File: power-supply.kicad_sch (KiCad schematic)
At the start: 107 parts, among them J10 Molex_Pico-Lock_1x2_504050-02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, J5 Molex_Pico-Lock_1x2_504050-02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, Q1 BSS138PW, Q2 BSS138PW, Q3 BSS138PW, Q4 BSS138PW, Q5 BSS138PW, Q6 BSS138PW, U10 TPS62823DLCT, U11 TPS62823DLCT, U12 TPS62823DLCT, U13 TPS62823DLCT, U16 TPS62823DLCT, U25 TPS54561QDPRRQ1, U9 LM3881

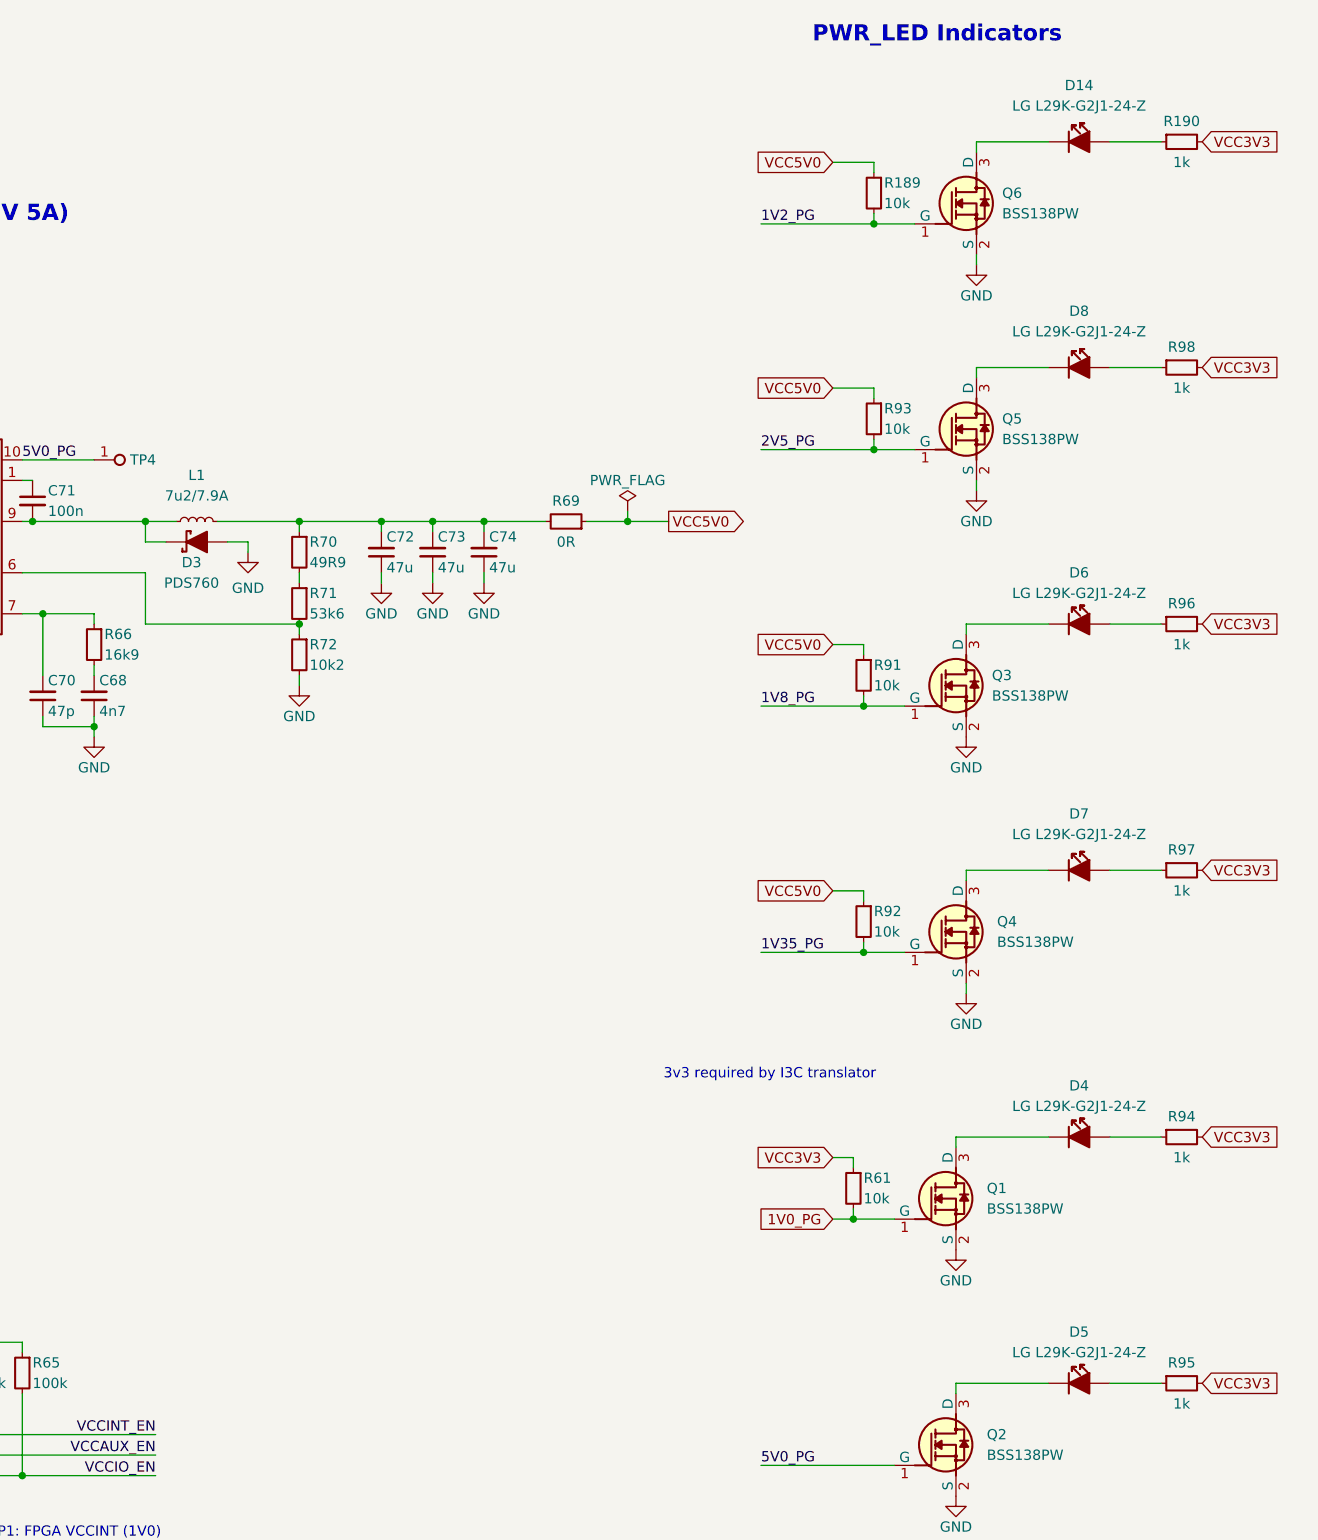
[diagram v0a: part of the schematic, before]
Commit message: [#68236] Update symbols and footprints, clean ERC and DRC
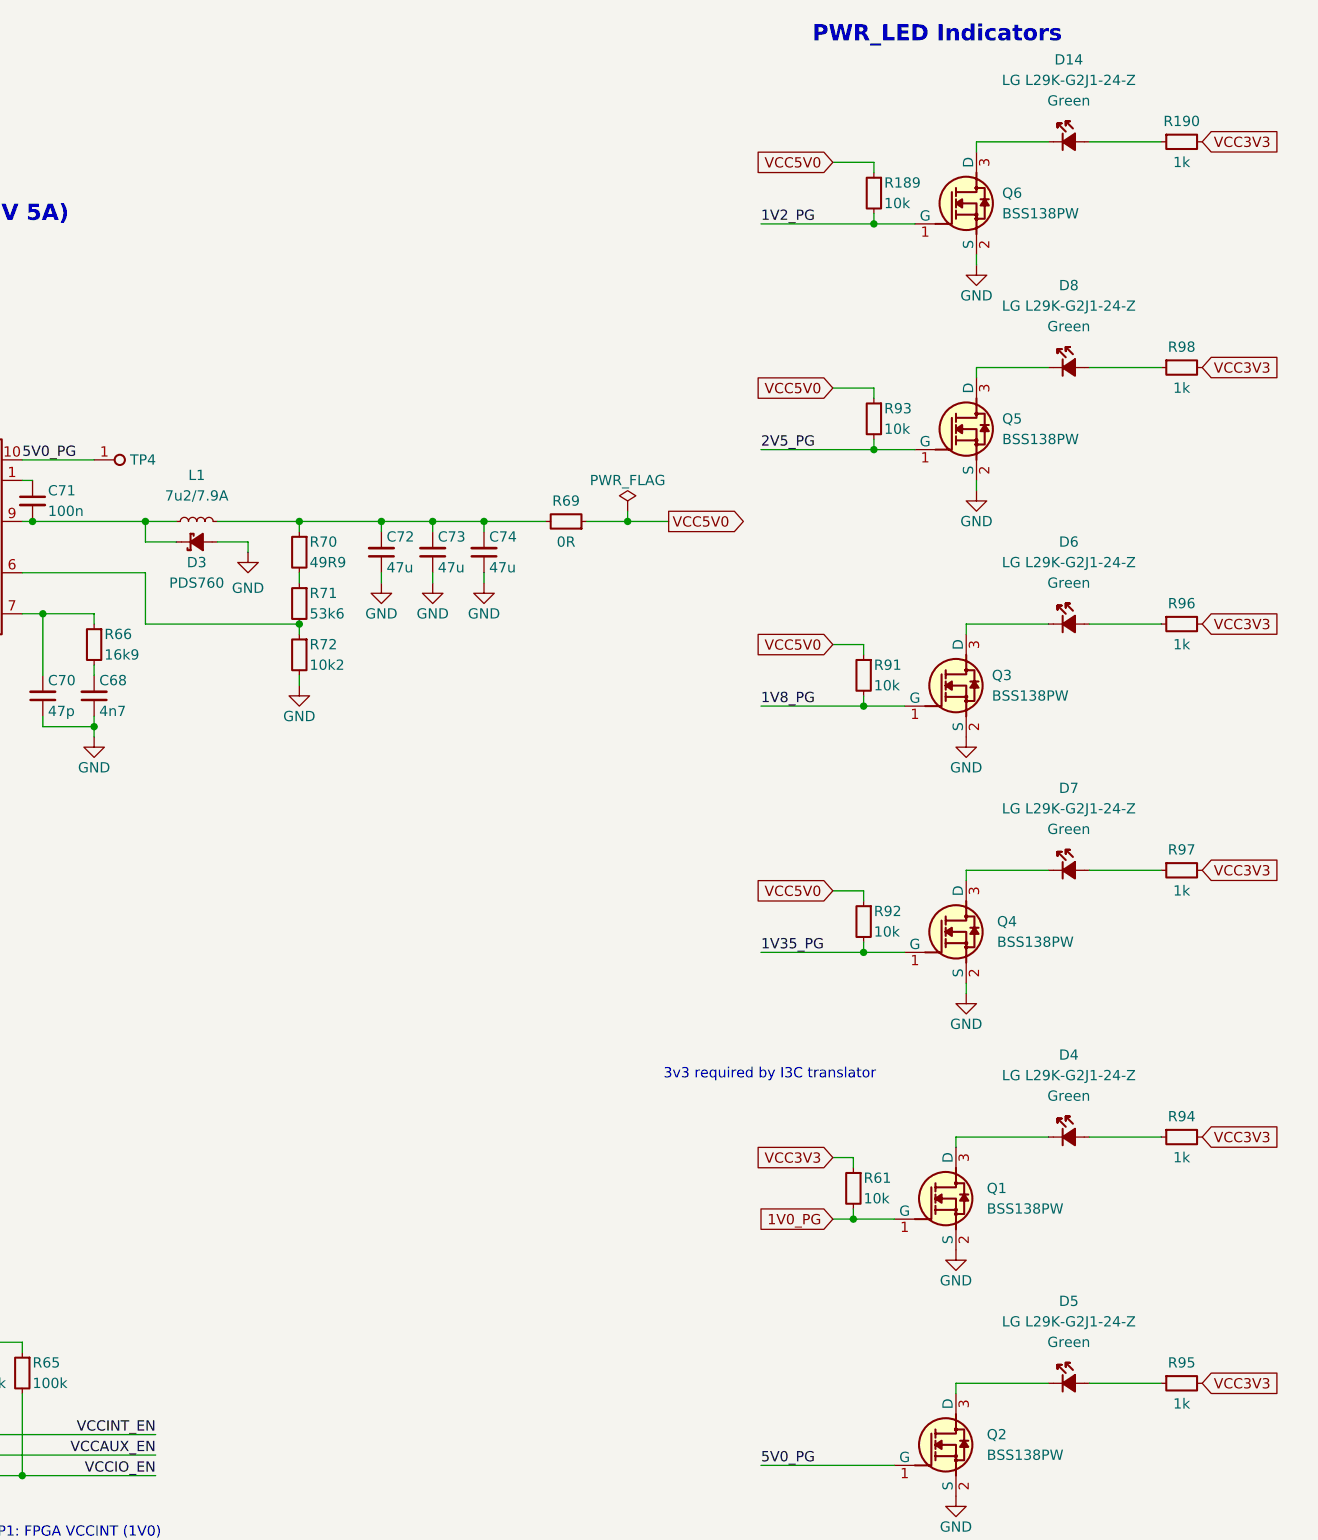
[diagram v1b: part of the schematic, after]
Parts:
- C2, C75, C76, C77, C78: Dielectric (none) -> template_dielectric
- C3, C79, C80, C81, C82: Dielectric (none) -> C0G; Voltage (none) -> 100V
- C65, C66, C67, C71: Public (none) -> False
- D14, D4, D5, D6, D7, D8: Color (none) -> Green
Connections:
- net GND: now also D3.2 (A); no longer D3.A
- net at R190.1: now also D14.2 (A); no longer D14.1
- net at Q6.3 (D): now also D14.1 (C); no longer D14.2
- net at Q3.3 (D): now also D6.1 (C); no longer D6.2
- net at Q4.3 (D): now also D7.1 (C); no longer D7.2
- net at Q1.3 (D): now also D4.1 (C); no longer D4.2
- net at Q2.3 (D): now also D5.1 (C); no longer D5.2
- net at Q5.3 (D): now also D8.1 (C); no longer D8.2
- net at C71.2, L1.1, U25.9 (SW): now also D3.1 (C); no longer D3.C
- net at R98.1: now also D8.2 (A); no longer D8.1
- net at R96.1: now also D6.2 (A); no longer D6.1
- net at R97.1: now also D7.2 (A); no longer D7.1
- net at R94.1: now also D4.2 (A); no longer D4.1
- net at R95.1: now also D5.2 (A); no longer D5.1

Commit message: [#82378] Project refresh 81589
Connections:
- net GND: now also J10.MP1 (MP), J10.MP2, J5.MP1 (MP), J5.MP2; no longer J10.SH, J5.SH
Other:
- moved on the sheet: C14, C15, C16, C65, C66, C67, R187, R190, R72, R74, R76, R78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

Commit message: a lot of routing and almost all caps of the fpga are placed down
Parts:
- C101, C103, C250, C3, C64, C68, C69, C70, C71, C79, C80, C81, C82, C83, C84, C85, C86, C87, C88, C89, C90: footprint antmicro-footprints:C_0402_1005Metric -> Capacitor_SMD:C_0402_1005Metric
- C14, C15, C16, C2, C65, C66, C67, C72, C73, C74, C75, C76, C77, C78: footprint antmicro-footprints:C_0603_1608Metric -> Capacitor_SMD:C_0603_1608Metric
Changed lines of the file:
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@@
 			)
 		)
-		(property "Footprint" "antmicro-footprints:C_0603_1608Metric"
+		(property "Footprint" "Capacitor_SMD:C_0603_1608Metric"
 			(at 328.93 187.96 0)
 			(hide yes)
@@
 			)
 		)
-		(property "Footprint" "antmicro-footprints:C_0402_1005Metric"
+		(property "Footprint" "Capacitor_SMD:C_0402_1005Metric"
 			(at 365.76 198.12 0)
 			(hide yes)
@@
 			)
 		)
-		(property "Footprint" "antmicro-footprints:C_0402_1005Metric"
+		(property "Footprint" "Capacitor_SMD:C_0402_1005Metric"
 			(at 382.27 198.12 0)
 			(hide yes)
@@
 			)
 		)
-		(property "Footprint" "antmicro-footprints:C_0402_1005Metric"
+		(property "Footprint" "Capacitor_SMD:C_0402_1005Metric"
 			(at 389.89 198.12 0)
 			(hide yes)
@@
 			)
 		)
-		(property "Footprint" "antmicro-footprints:C_0402_1005Metric"
+		(property "Footprint" "Capacitor_SMD:C_0402_1005Metric"
 			(at 74.93 187.96 0)
 			(hide yes)
@@
 			)
 		)
-		(property "Footprint" "antmicro-footprints:C_0603_1608Metric"
+		(property "Footprint" "Capacitor_SMD:C_0603_1608Metric"
 			(at 87.63 43.18 0)
 			(hide yes)
@@
 			)
 		)
-		(property "Footprint" "antmicro-footprints:C_0603_1608Metric"
+		(property "Footprint" "Capacitor_SMD:C_0603_1608Metric"
 			(at 93.98 43.18 0)
 			(hide yes)
@@
 			)
 		)
-		(property "Footprint" "antmicro-footprints:C_0603_1608Metric"
+		(property "Footprint" "Capacitor_SMD:C_0603_1608Metric"
 			(at 100.33 43.18 0)
 			(hide yes)
@@
 			)
 		)
-		(property "Footprint" "antmicro-footprints:C_0402_1005Metric"
+		(property "Footprint" "Capacitor_SMD:C_0402_1005Metric"
 			(at 101.6 69.85 0)
 			(hide yes)
@@
 			)
 		)
-		(property "Footprint" "antmicro-footprints:C_0402_1005Metric"
+		(property "Footprint" "Capacitor_SMD:C_0402_1005Metric"
 			(at 142.24 85.09 0)
 			(hide yes)
@@
 			)
 		)
-		(property "Footprint" "antmicro-footprints:C_0402_1005Metric"
+		(property "Footprint" "Capacitor_SMD:C_0402_1005Metric"
 			(at 135.89 85.09 0)
 			(hide yes)
@@
 			)
 		)
-		(property "Footprint" "antmicro-footprints:C_0402_1005Metric"
+		(property "Footprint" "Capacitor_SMD:C_0402_1005Metric"
 			(at 109.22 96.52 0)
 			(hide yes)
@@
 			)
 		)
-		(property "Footprint" "antmicro-footprints:C_0603_1608Metric"
+		(property "Footprint" "Capacitor_SMD:C_0603_1608Metric"
 			(at 177.8 67.31 0)
 			(hide yes)
@@
 			)
 		)
-		(property "Footprint" "antmicro-footprints:C_0603_1608Metric"
+		(property "Footprint" "Capacitor_SMD:C_0603_1608Metric"
 			(at 184.15 67.31 0)
 			(hide yes)
@@
 			)
 		)
-		(property "Footprint" "antmicro-footprints:C_0603_1608Metric"
+		(property "Footprint" "Capacitor_SMD:C_0603_1608Metric"
 			(at 190.5 67.31 0)
 			(hide yes)
@@
 			)
 		)
-		(property "Footprint" "antmicro-footprints:C_0603_1608Metric"
+		(property "Footprint" "Capacitor_SMD:C_0603_1608Metric"
 			(at 328.93 10.16 0)
 			(hide yes)
@@
 			)
 		)
-		(property "Footprint" "antmicro-footprints:C_0603_1608Metric"
+		(property "Footprint" "Capacitor_SMD:C_0603_1608Metric"
 			(at 57.15 43.18 0)
 			(hide yes)
@@
 			)
 		)
-		(property "Footprint" "antmicro-footprints:C_0603_1608Metric"
+		(property "Footprint" "Capacitor_SMD:C_0603_1608Metric"
 			(at 67.31 43.18 0)
 			(hide yes)
@@
 			)
 		)
-		(property "Footprint" "antmicro-footprints:C_0603_1608Metric"
+		(property "Footprint" "Capacitor_SMD:C_0603_1608Metric"
 			(at 77.47 43.18 0)
 			(hide yes)
@@
 			)
 		)
-		(property "Footprint" "antmicro-footprints:C_0402_1005Metric"
+		(property "Footprint" "Capacitor_SMD:C_0402_1005Metric"
 			(at 365.76 20.32 0)
 			(hide yes)
@@
 			)
 		)
-		(property "Footprint" "antmicro-footprints:C_0402_1005Metric"
+		(property "Footprint" "Capacitor_SMD:C_0402_1005Metric"
 			(at 85.09 187.96 0)
 			(hide yes)
@@
 			)
 		)
-		(property "Footprint" "antmicro-footprints:C_0402_1005Metric"
+		(property "Footprint" "Capacitor_SMD:C_0402_1005Metric"
 			(at 382.27 20.32 0)
 			(hide yes)
@@
 			)
 		)
-		(property "Footprint" "antmicro-footprints:C_0402_1005Metric"
+		(property "Footprint" "Capacitor_SMD:C_0402_1005Metric"
 			(at 389.89 20.32 0)
 			(hide yes)
@@
 			)
 		)
-		(property "Footprint" "antmicro-footprints:C_0603_1608Metric"
+		(property "Footprint" "Capacitor_SMD:C_0603_1608Metric"
 			(at 328.93 54.61 0)
 			(hide yes)
@@
 			)
 		)
-		(property "Footprint" "antmicro-footprints:C_0402_1005Metric"
+		(property "Footprint" "Capacitor_SMD:C_0402_1005Metric"
 			(at 365.76 64.77 0)
 			(hide yes)
@@
 			)
 		)
-		(property "Footprint" "antmicro-footprints:C_0402_1005Metric"
+		(property "Footprint" "Capacitor_SMD:C_0402_1005Metric"
 			(at 382.27 64.77 0)
 			(hide yes)
@@
 			)
 		)
-		(property "Footprint" "antmicro-footprints:C_0402_1005Metric"
+		(property "Footprint" "Capacitor_SMD:C_0402_1005Metric"
 			(at 389.89 64.77 0)
 			(hide yes)
@@
 			)
 		)
-		(property "Footprint" "antmicro-footprints:C_0603_1608Metric"
+		(property "Footprint" "Capacitor_SMD:C_0603_1608Metric"
 			(at 328.93 99.06 0)
 			(hide yes)
@@
 			)
 		)
-		(property "Footprint" "antmicro-footprints:C_0402_1005Metric"
+		(property "Footprint" "Capacitor_SMD:C_0402_1005Metric"
 			(at 365.76 109.22 0)
 			(hide yes)
@@
 			)
 		)
-		(property "Footprint" "antmicro-footprints:C_0402_1005Metric"
+		(property "Footprint" "Capacitor_SMD:C_0402_1005Metric"
 			(at 382.27 109.22 0)
 			(hide yes)
@@
 			)
 		)
-		(property "Footprint" "antmicro-footprints:C_0402_1005Metric"
+		(property "Footprint" "Capacitor_SMD:C_0402_1005Metric"
 			(at 389.89 109.22 0)
 			(hide yes)
@@
 			)
 		)
-		(property "Footprint" "antmicro-footprints:C_0603_1608Metric"
+		(property "Footprint" "Capacitor_SMD:C_0603_1608Metric"
 			(at 328.93 143.51 0)
 			(hide yes)
@@
 			)
 		)
-		(property "Footprint" "antmicro-footprints:C_0402_1005Metric"
+		(property "Footprint" "Capacitor_SMD:C_0402_1005Metric"
 			(at 365.76 153.67 0)
 			(hide yes)
@@
 			)
 		)
-		(property "Footprint" "antmicro-footprints:C_0402_1005Metric"
+		(property "Footprint" "Capacitor_SMD:C_0402_1005Metric"
 			(at 382.27 153.67 0)
 			(hide yes)
@@
 			)
 		)
-		(property "Footprint" "antmicro-footprints:C_0402_1005Metric"
+		(property "Footprint" "Capacitor_SMD:C_0402_1005Metric"
 			(at 389.89 153.67 0)
 			(hide yes)

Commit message: bom changes
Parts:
- R138, R14, R15, R16, R185: MPN ERJ2GE0R00X -> RC0402JR-7D0RL; Manufacturer Panasonic -> YAGEO

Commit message: version 1.0 complete
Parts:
- C2, C75, C76, C77, C78: MPN GRM188R61A106KE69D -> GRT188R61A106KE13D
- C68: MPN CGA2B3X7S2A472K050BB -> CC0402KRX7R0BB472; Manufacturer TDK -> YAGEO
- D14, D4, D5, D6, D7, D8: MPN LG L29K-G2J1-24-Z -> SML-D13FWT86C; Manufacturer OSRAM -> ROHM Semiconductor
- L2, L3, L4, L5, L6: MPN IHLP1212AEERR47M11 -> IHLP1212AEEZR47M1Z
- Q1, Q2, Q3, Q4, Q5, Q6: MPN BSS138PW -> BSS138BKW,115
- R189, R61, R91, R92, R93: MPN CR0402-FX-1002GLF -> CR0402AFX-1002GAS
- R69: MPN MCMR12X000_PTL -> CRCW12060000Z0EAHP; Manufacturer Multicomp Pro -> Vishay

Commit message: "In the process of upgrading the ddr memory"
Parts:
- removed J10: Molex_Pico-Lock_1x2_504050-0291, antmicro-footprints:Conn_Molex_Pico-Lock_1x2_504050-0291, symbol antmicroWire2BoardConnectors:Molex_Pico-Lock_1x2_504050-0291
- R138, R14, R15, R16, R185, R186, R187, R189, R190, R61, R63, R64, R65, R66, R67, R68, R70, R71, R72, R73, R74, R75, R76, R77, R78, R79, R80, R91, R92, R93, R94, R95, R96, R97, R98: footprint antmicro-footprints:R_0402_1005Metric -> Resistor_SMD:R_0402_1005Metric
- R139, R140, R141, R142, R188: footprint antmicro-footprints:R_0603_1608Metric -> Resistor_SMD:R_0603_1608Metric
- R69: footprint antmicro-footprints:R_1206_3216Metric -> Resistor_SMD:R_1206_3216Metric
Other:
- note removed: "Battery connector"
- note removed: "To DC-SCM connector"
- moved on the sheet: C250, C64, R63, R64, R65, R68, U9
